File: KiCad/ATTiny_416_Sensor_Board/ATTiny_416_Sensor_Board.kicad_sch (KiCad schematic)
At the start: 0 parts

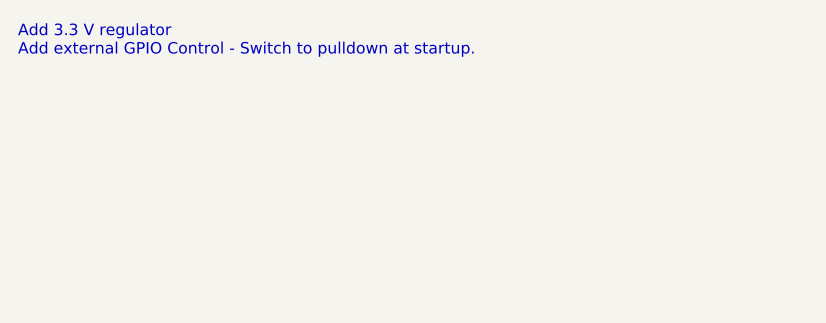
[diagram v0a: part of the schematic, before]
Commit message: removed bad schematic notes and re-plotted
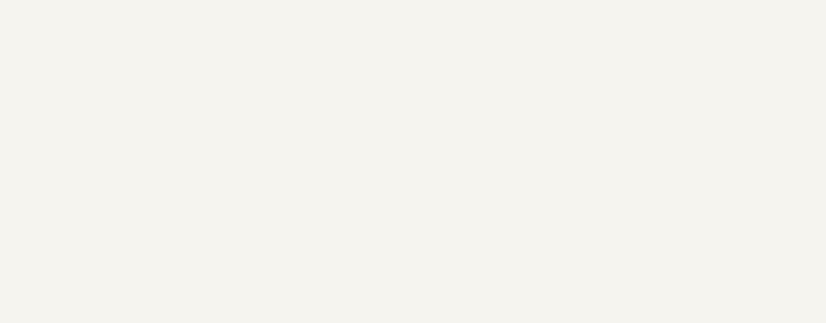
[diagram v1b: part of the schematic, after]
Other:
- note removed: "Add 3.3 V regulator Add external GPIO Control - Switch to pulldown at startup."
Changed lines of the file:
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@@
 		(title "ATTiny416 Development Board")
 		(date "2025-02-09")
-		(rev "1")
-	)
-	(text "Add 3.3 V regulator\nAdd external GPIO Control - Switch to pulldown at startup."
-		(exclude_from_sim no)
-		(at 25.146 29.21 0)
-		(effects
-			(font
-				(size 1.27 1.27)
-			)
-			(justify left)
-		)
+		(rev "2")
 	)
 	(sheet
